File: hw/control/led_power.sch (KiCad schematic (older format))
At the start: 19 parts, among them Q601 BC817, Q602 BC807, U401 LM2678T-ADJ

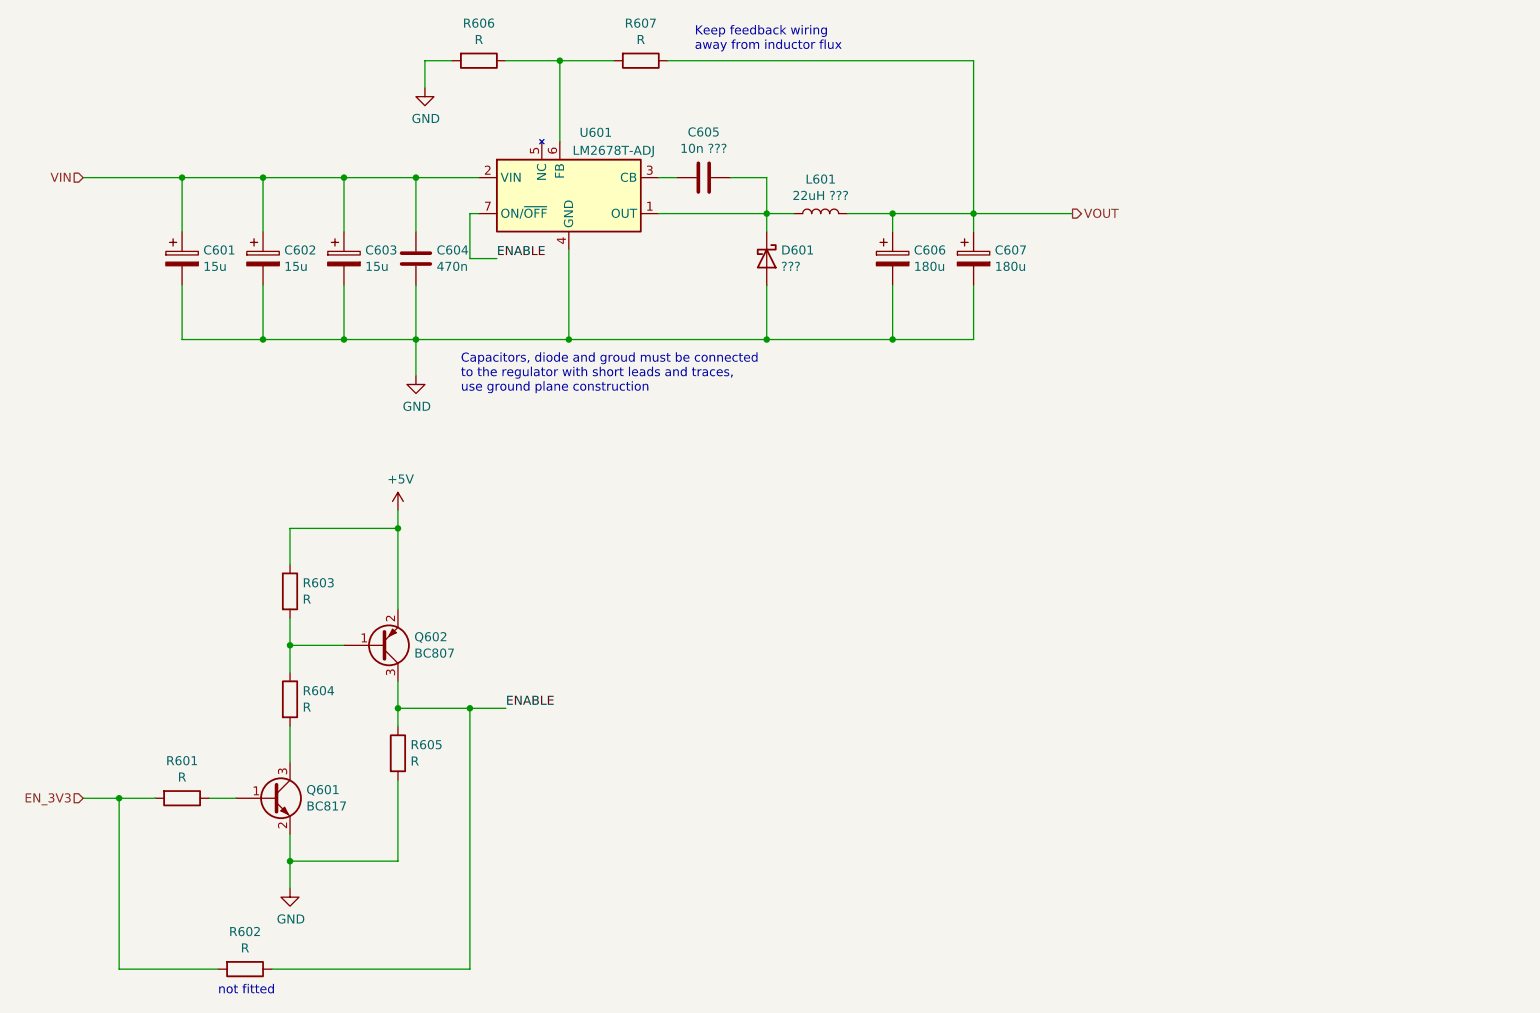
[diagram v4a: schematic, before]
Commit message: [hw] Add notes on LED power coil selection
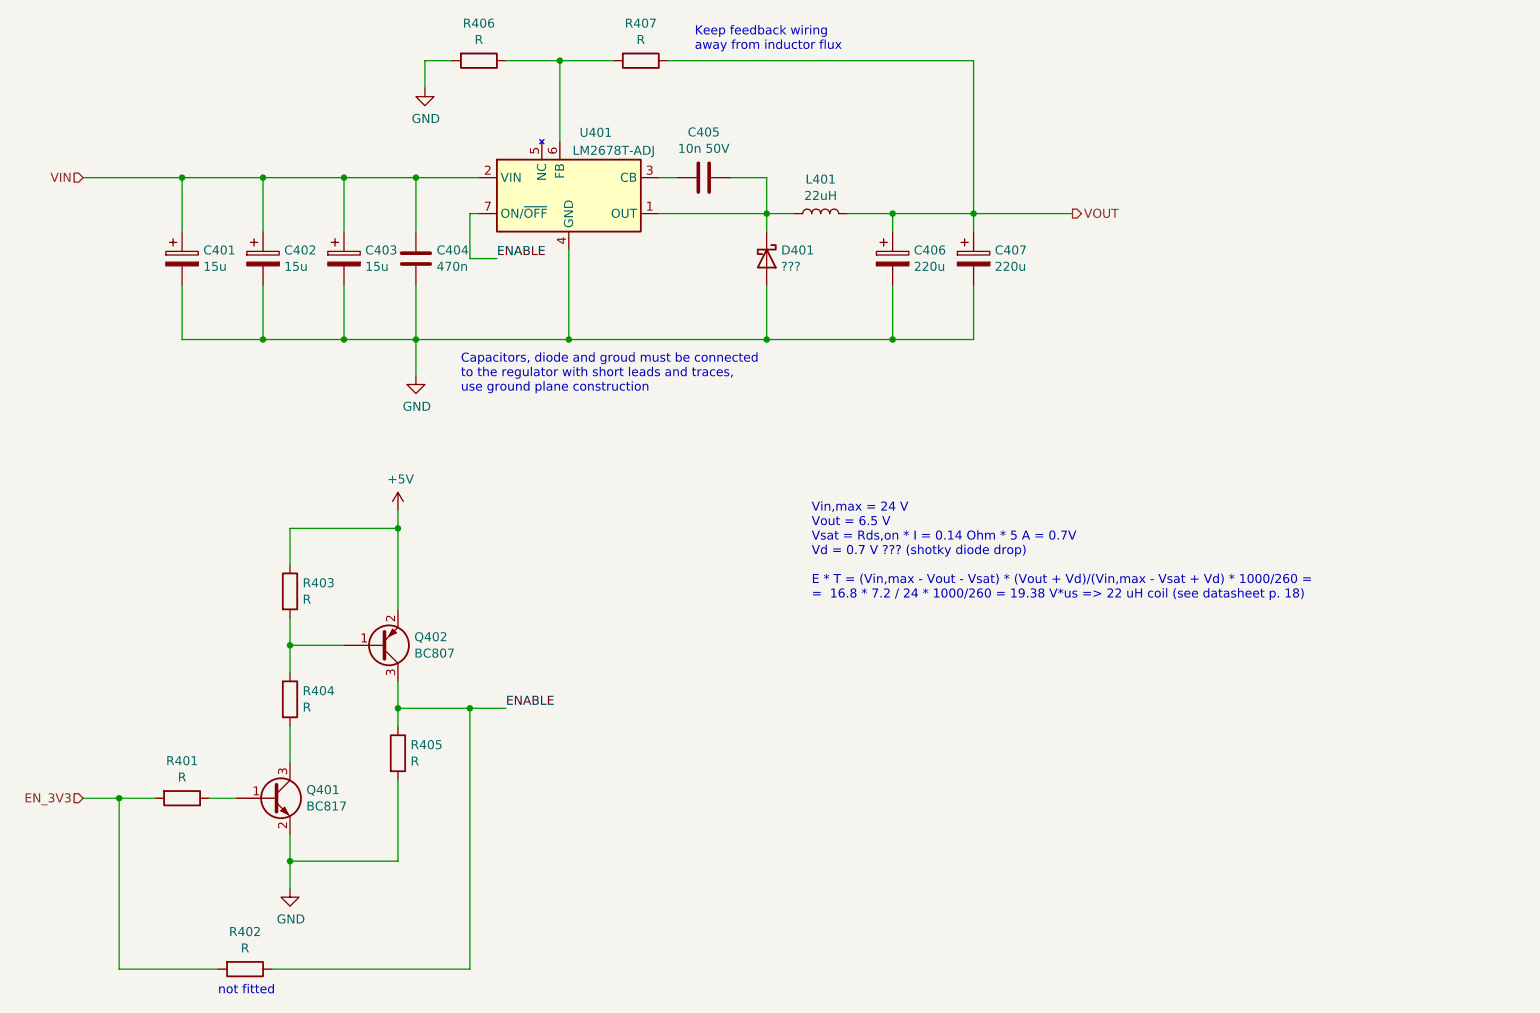
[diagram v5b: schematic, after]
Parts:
- C405: value 10n ??? -> 10n 50V
- C606, C607: value 180u -> 220u
- L601: value 22uH ??? -> 22uH
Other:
- note added: "Vin,max = 24 V\nVout = 6.5 V\nVsat = Rds,on * I = 0.14 Ohm * 5 A = 0.7V\nVd = 0.7 V ??? (shotky diode drop)\n\nE * T = (Vin,max - Vout - Vsat) * (Vout + Vd)/(Vin,max - Vsat + Vd) * 1000/260 = \n= 16.8 * 7.2 / 24 * 1000/260 = 19.38 V*us => 22 uH coil (see datasheet p. 18)"
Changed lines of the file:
@@
 $Descr A4 11693 8268
 encoding utf-8
-Sheet 6 9
+Sheet 4 9
 Title "WS2812 Controller"
 Date "2021-09-21"
@@
 AR Path="/614AB031/6145ECF0" Ref="U401"  Part="1"
 AR Path="/614AE8DA/6145ECF0" Ref="U601"  Part="1"
-F 0 "U601" H 5550 2750 50  0000 C CNN
+F 0 "U401" H 5550 2750 50  0000 C CNN
 F 1 "LM2678T-ADJ" H 5650 2650 50  0000 C CNN
 F 2 "Package_TO_SOT_THT:TO-220-7_P2.54x3.7mm_StaggerOdd_Lead3.8mm_Vertical" H 5450 2150 50  0001 L CIN
@@
 AR Path="/614AB031/6145FC0F" Ref="C405"  Part="1"
 AR Path="/614AE8DA/6145FC0F" Ref="C605"  Part="1"
-F 0 "C605" V 5898 2300 50  0000 C CNN
-F 1 "10n ???" V 5989 2300 50  0000 C CNN
+F 0 "C405" V 5898 2300 50  0000 C CNN
+F 1 "10n 50V" V 5989 2300 50  0000 C CNN
 F 2 "" H 6188 2150 50  0001 C CNN
 F 3 "~" H 6150 2300 50  0001 C CNN
@@
 AR Path="/614AB031/61460B18" Ref="#PWR0403"  Part="1"
 AR Path="/614AE8DA/61460B18" Ref="#PWR0603"  Part="1"
-F 0 "#PWR0603" H 4550 3150 50  0001 C CNN
+F 0 "#PWR0403" H 4550 3150 50  0001 C CNN
 F 1 "GND" H 4555 3227 50  0000 C CNN
 F 2 "" H 4550 3400 50  0001 C CNN
@@
 AR Path="/614AE8DA/61461C6E" Ref="D601"  Part="1"
 AR Path="/614AB031/61461C6E" Ref="D401"  Part="1"
-F 0 "D601" V 6454 2830 50  0000 L CNN
+F 0 "D401" V 6454 2830 50  0000 L CNN
 F 1 "???" V 6545 2830 50  0000 L CNN
 F 2 "" H 6500 2750 50  0001 C CNN
@@
 AR Path="/614AE8DA/61462D51" Ref="L601"  Part="1"
 AR Path="/614AB031/61462D51" Ref="L401"  Part="1"
-F 0 "L601" V 6990 2500 50  0000 C CNN
-F 1 "22uH ???" V 6899 2500 50  0000 C CNN
+F 0 "L401" V 6990 2500 50  0000 C CNN
+F 1 "22uH" V 6899 2500 50  0000 C CNN
 F 2 "" H 6800 2500 50  0001 C CNN
 F 3 "~" H 6800 2500 50  0001 C CNN
@@
 AR Path="/614AE8DA/61463CC3" Ref="C606"  Part="1"
 AR Path="/614AB031/61463CC3" Ref="C406"  Part="1"
-F 0 "C606" H 7318 2796 50  0000 L CNN
-F 1 "180u" H 7318 2705 50  0000 L CNN
+F 0 "C406" H 7318 2796 50  0000 L CNN
+F 1 "220u" H 7318 2705 50  0000 L CNN
 F 2 "" H 7238 2600 50  0001 C CNN
 F 3 "~" H 7200 2750 50  0001 C CNN
@@
 AR Path="/614AE8DA/6146511A" Ref="C607"  Part="1"
 AR Path="/614AB031/6146511A" Ref="C407"  Part="1"
-F 0 "C607" H 7768 2796 50  0000 L CNN
-F 1 "180u" H 7768 2705 50  0000 L CNN
+F 0 "C407" H 7768 2796 50  0000 L CNN
+F 1 "220u" H 7768 2705 50  0000 L CNN
 F 2 "" H 7688 2600 50  0001 C CNN
 F 3 "~" H 7650 2750 50  0001 C CNN
@@
 AR Path="/614AE8DA/61465477" Ref="C603"  Part="1"
 AR Path="/614AB031/61465477" Ref="C403"  Part="1"
-F 0 "C603" H 4268 2796 50  0000 L CNN
+F 0 "C403" H 4268 2796 50  0000 L CNN
 F 1 "15u" H 4268 2705 50  0000 L CNN
 F 2 "" H 4188 2600 50  0001 C CNN
@@
 AR Path="/614AE8DA/614679D1" Ref="C602"  Part="1"
 AR Path="/614AB031/614679D1" Ref="C402"  Part="1"
-F 0 "C602" H 3818 2796 50  0000 L CNN
+F 0 "C402" H 3818 2796 50  0000 L CNN
 F 1 "15u" H 3818 2705 50  0000 L CNN
 F 2 "" H 3738 2600 50  0001 C CNN
@@
 AR Path="/614AE8DA/61467CFC" Ref="C601"  Part="1"
 AR Path="/614AB031/61467CFC" Ref="C401"  Part="1"
-F 0 "C601" H 3368 2796 50  0000 L CNN
+F 0 "C401" H 3368 2796 50  0000 L CNN
 F 1 "15u" H 3368 2705 50  0000 L CNN
 F 2 "" H 3288 2600 50  0001 C CNN
@@
 AR Path="/614AE8DA/614681BF" Ref="C604"  Part="1"
 AR Path="/614AB031/614681BF" Ref="C404"  Part="1"
-F 0 "C604" H 4665 2796 50  0000 L CNN
+F 0 "C404" H 4665 2796 50  0000 L CNN
 F 1 "470n" H 4665 2705 50  0000 L CNN
 F 2 "" H 4588 2600 50  0001 C CNN
@@
 AR Path="/614AE8DA/6147393D" Ref="R607"  Part="1"
 AR Path="/614AB031/6147393D" Ref="R407"  Part="1"
-F 0 "R607" V 5593 1650 50  0000 C CNN
+F 0 "R407" V 5593 1650 50  0000 C CNN
 F 1 "R" V 5684 1650 50  0000 C CNN
 F 2 "" V 5730 1650 50  0001 C CNN
@@
 AR Path="/614AE8DA/61475A47" Ref="R606"  Part="1"
 AR Path="/614AB031/61475A47" Ref="R406"  Part="1"
-F 0 "R606" V 4693 1650 50  0000 C CNN
+F 0 "R406" V 4693 1650 50  0000 C CNN
 F 1 "R" V 4784 1650 50  0000 C CNN
 F 2 "" V 4830 1650 50  0001 C CNN
@@
 AR Path="/614AE8DA/61477A40" Ref="#PWR0604"  Part="1"
 AR Path="/614AB031/61477A40" Ref="#PWR0404"  Part="1"
-F 0 "#PWR0604" H 4600 1550 50  0001 C CNN
+F 0 "#PWR0404" H 4600 1550 50  0001 C CNN
 F 1 "GND" H 4605 1627 50  0000 C CNN
 F 2 "" H 4600 1800 50  0001 C CNN
@@
 AR Path="/614AE8DA/6147DB7E" Ref="R601"  Part="1"
 AR Path="/614AB031/6147DB7E" Ref="R401"  Part="1"
-F 0 "R601" V 3043 5750 50  0000 C CNN
+F 0 "R401" V 3043 5750 50  0000 C CNN
 F 1 "R" V 3134 5750 50  0000 C CNN
 F 2 "" V 3180 5750 50  0001 C CNN
@@
 AR Path="/614AE8DA/6147EFCD" Ref="Q601"  Part="1"
 AR Path="/614AB031/6147EFCD" Ref="Q401"  Part="1"
-F 0 "Q601" H 3941 5796 50  0000 L CNN
+F 0 "Q401" H 3941 5796 50  0000 L CNN
 F 1 "BC817" H 3941 5705 50  0000 L CNN
 F 2 "" H 3950 5850 50  0001 C CNN
@@
 AR Path="/614AE8DA/61480A0D" Ref="Q602"  Part="1"
 AR Path="/614AB031/61480A0D" Ref="Q402"  Part="1"
-F 0 "Q602" H 4541 4854 50  0000 L CNN
+F 0 "Q402" H 4541 4854 50  0000 L CNN
 F 1 "BC807" H 4541 4945 50  0000 L CNN
 F 2 "" H 4550 5000 50  0001 C CNN
@@
 AR Path="/614AE8DA/6148128F" Ref="R604"  Part="1"
 AR Path="/614AB031/6148128F" Ref="R404"  Part="1"
-F 0 "R604" H 3920 5246 50  0000 L CNN
+F 0 "R404" H 3920 5246 50  0000 L CNN
 F 1 "R" H 3920 5155 50  0000 L CNN
 F 2 "" V 3780 5200 50  0001 C CNN
@@
 AR Path="/614AE8DA/614817B0" Ref="R603"  Part="1"
 AR Path="/614AB031/614817B0" Ref="R403"  Part="1"
-F 0 "R603" H 3920 4646 50  0000 L CNN
+F 0 "R403" H 3920 4646 50  0000 L CNN
 F 1 "R" H 3920 4555 50  0000 L CNN
 F 2 "" V 3780 4600 50  0001 C CNN
@@
 AR Path="/614AE8DA/61483286" Ref="#PWR0601"  Part="1"
 AR Path="/614AB031/61483286" Ref="#PWR0401"  Part="1"
-F 0 "#PWR0601" H 3850 6000 50  0001 C CNN
+F 0 "#PWR0401" H 3850 6000 50  0001 C CNN
 F 1 "GND" H 3855 6077 50  0000 C CNN
 F 2 "" H 3850 6250 50  0001 C CNN
@@
 AR Path="/614AE8DA/61486663" Ref="#PWR0602"  Part="1"
 AR Path="/614AB031/61486663" Ref="#PWR0402"  Part="1"
-F 0 "#PWR0602" H 4450 4000 50  0001 C CNN
+F 0 "#PWR0402" H 4450 4000 50  0001 C CNN
 F 1 "+5V" H 4465 4323 50  0000 C CNN
 F 2 "" H 4450 4150 50  0001 C CNN
@@
 AR Path="/614AE8DA/6148D73D" Ref="R605"  Part="1"
 AR Path="/614AB031/6148D73D" Ref="R405"  Part="1"
-F 0 "R605" H 4520 5546 50  0000 L CNN
+F 0 "R405" H 4520 5546 50  0000 L CNN
 F 1 "R" H 4520 5455 50  0000 L CNN
 F 2 "" V 4380 5500 50  0001 C CNN
@@
 AR Path="/614AE8DA/614CC1BE" Ref="R602"  Part="1"
 AR Path="/614AB031/614CC1BE" Ref="R402"  Part="1"
-F 0 "R602" V 3393 6700 50  0000 C CNN
+F 0 "R402" V 3393 6700 50  0000 C CNN
 F 1 "R" V 3484 6700 50  0000 C CNN
 F 2 "" V 3530 6700 50  0001 C CNN
@@
 Wire Wire Line
 	2900 5750 3100 5750
+Text Notes 6750 4650 0    50   ~ 0
+Vin,max = 24 V\nVout = 6.5 V\nVsat = Rds,on * I = 0.14 Ohm * 5 A = 0.7V\nVd = 0.7 V ??? (shotky diode drop)\n\nE * T = (Vin,max - Vout - Vsat) * (Vout + Vd)/(Vin,max - Vsat + Vd) * 1000/260 = \n=  16.8 * 7.2 / 24 * 1000/260 = 19.38 V*us => 22 uH coil (see datasheet p. 18)
 $EndSCHEMATC

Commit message: [hw] Add some more peripherals
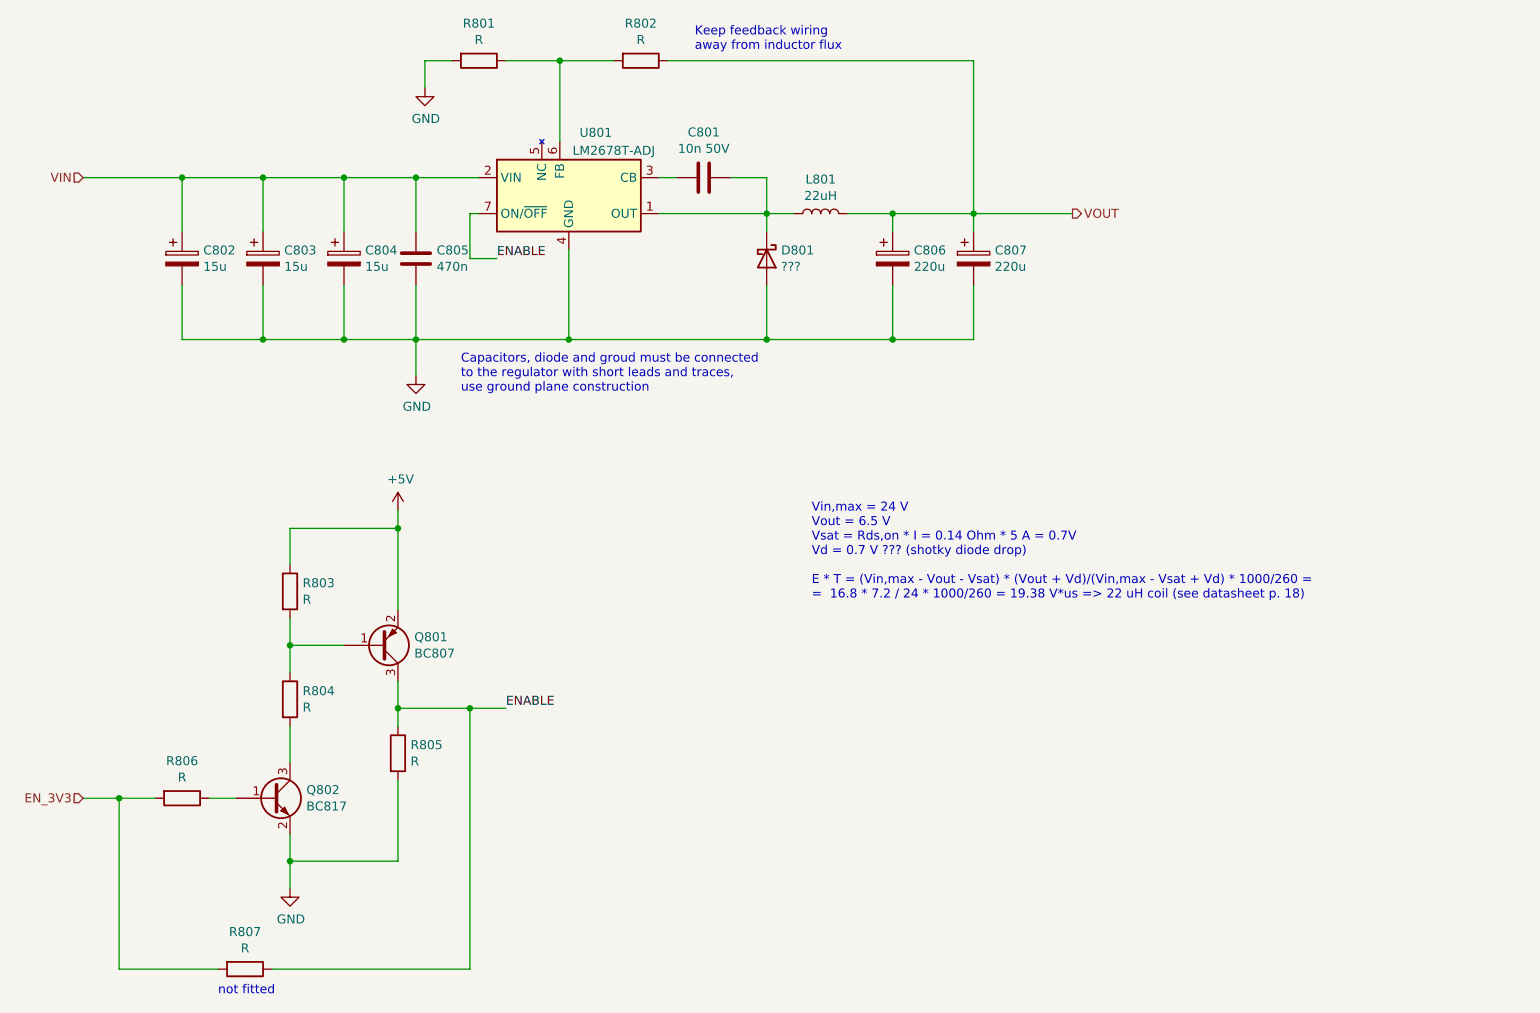
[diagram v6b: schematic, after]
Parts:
- renumbered C601 to C1002, C602 to C1003, C603 to C1004, C604 to C1005, C606 to C1006, C607 to C1007, C405 to C801, D601 to D1001, L601 to L1001, Q602 to Q1001, Q601 to Q1002, R606 to R1001, R607 to R1002, R603 to R1003, R604 to R1004, R605 to R1005, R601 to R1006, R602 to R1007, U401 to U801
